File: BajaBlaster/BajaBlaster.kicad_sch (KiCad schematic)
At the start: 0 parts

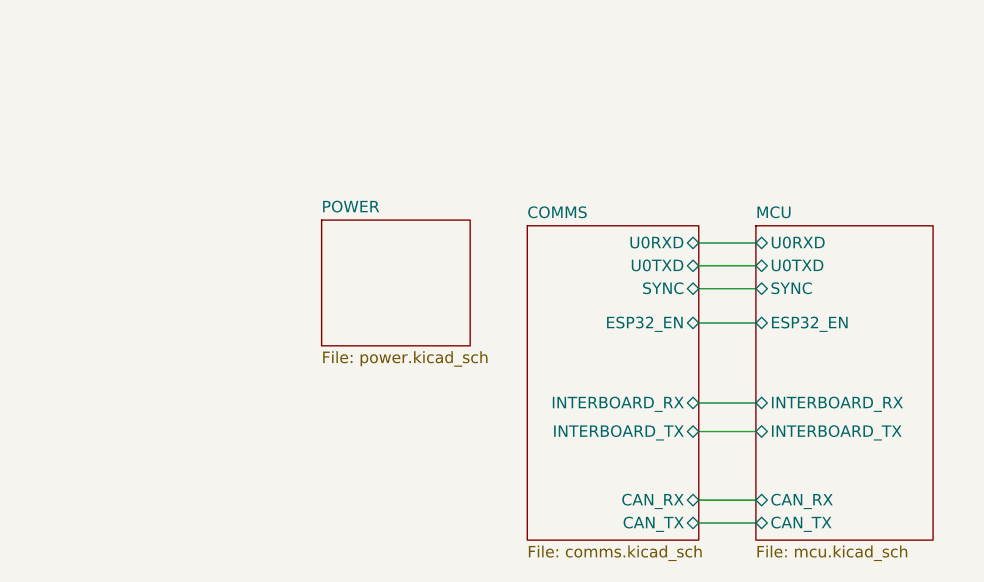
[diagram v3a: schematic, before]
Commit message: added better formatting across schematic
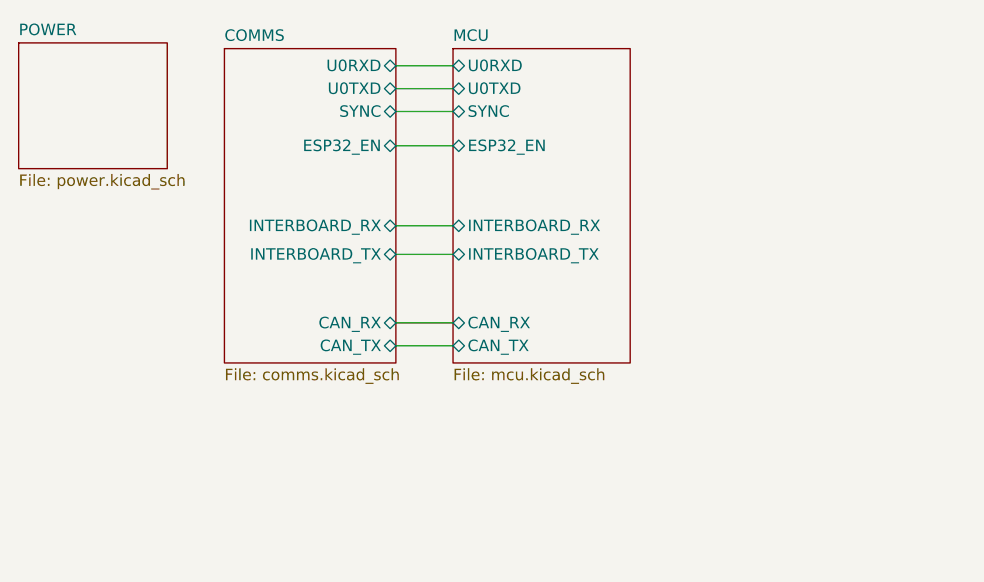
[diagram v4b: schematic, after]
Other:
- company: (none) -> Olin Baja SAE
- title: BAJA_BLASTER_REV_A -> BAJA_BLASTER
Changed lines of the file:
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@@
 	(paper "A5")
 	(title_block
-		(title "BAJA_BLASTER_REV_A")
-	)
-	(wire
-		(pts
-			(xy 99.06 60.96) (xy 105.41 60.96)
-		)
-		(stroke
-			(width 0)
-			(type default)
-		)
-	)
-	(wire
-		(pts
-			(xy 99.06 71.755) (xy 105.41 71.755)
-		)
-		(stroke
-			(width 0)
-			(type default)
-		)
-	)
-	(wire
-		(pts
-			(xy 99.06 48.26) (xy 105.41 48.26)
-		)
-		(stroke
-			(width 0)
-			(type default)
-		)
-	)
-	(wire
-		(pts
-			(xy 99.06 64.135) (xy 105.41 64.135)
-		)
-		(stroke
-			(width 0)
-			(type default)
-		)
-	)
-	(wire
-		(pts
-			(xy 99.06 74.295) (xy 105.41 74.295)
-		)
-		(stroke
-			(width 0)
-			(type default)
-		)
-	)
-	(wire
-		(pts
-			(xy 99.06 52.07) (xy 105.41 52.07)
-		)
-		(stroke
-			(width 0)
-			(type default)
-		)
-	)
-	(wire
-		(pts
-			(xy 99.06 43.18) (xy 105.41 43.18)
-		)
-		(stroke
-			(width 0)
-			(type default)
-		)
-	)
-	(wire
-		(pts
-			(xy 99.06 45.72) (xy 105.41 45.72)
+		(title "BAJA_BLASTER")
+		(date "2026-09-24")
+		(rev "A")
+		(company "Olin Baja SAE")
+	)
+	(wire
+		(pts
+			(xy 65.405 41.275) (xy 71.755 41.275)
+		)
+		(stroke
+			(width 0)
+			(type default)
+		)
+	)
+	(wire
+		(pts
+			(xy 65.405 52.07) (xy 71.755 52.07)
+		)
+		(stroke
+			(width 0)
+			(type default)
+		)
+	)
+	(wire
+		(pts
+			(xy 65.405 28.575) (xy 71.755 28.575)
+		)
+		(stroke
+			(width 0)
+			(type default)
+		)
+	)
+	(wire
+		(pts
+			(xy 65.405 44.45) (xy 71.755 44.45)
+		)
+		(stroke
+			(width 0)
+			(type default)
+		)
+	)
+	(wire
+		(pts
+			(xy 65.405 54.61) (xy 71.755 54.61)
+		)
+		(stroke
+			(width 0)
+			(type default)
+		)
+	)
+	(wire
+		(pts
+			(xy 65.405 32.385) (xy 71.755 32.385)
+		)
+		(stroke
+			(width 0)
+			(type default)
+		)
+	)
+	(wire
+		(pts
+			(xy 65.405 23.495) (xy 71.755 23.495)
+		)
+		(stroke
+			(width 0)
+			(type default)
+		)
+	)
+	(wire
+		(pts
+			(xy 65.405 26.035) (xy 71.755 26.035)
 		)
 		(stroke
@@
 	)
 	(sheet
-		(at 80.01 41.275)
+		(at 46.355 21.59)
 		(size 19.05 34.925)
 		(exclude_from_sim no)
@@
 		)
 		(property "Sheetname" "COMMS"
-			(at 80.01 40.5634 0)
+			(at 46.355 20.8784 0)
 			(show_name no)
 			(do_not_autoplace no)
@@
 		)
 		(property "Sheetfile" "comms.kicad_sch"
-			(at 80.01 76.7846 0)
+			(at 46.355 57.0996 0)
 			(show_name no)
 			(do_not_autoplace no)
@@
 		)
 		(pin "ESP32_EN" bidirectional
-			(at 99.06 52.07 0)
+			(at 65.405 32.385 0)
 			(effects
 				(font
@@
 		)
 		(pin "CAN_TX" bidirectional
-			(at 99.06 74.295 0)
+			(at 65.405 54.61 0)
 			(effects
 				(font
@@
 		)
 		(pin "CAN_RX" bidirectional
-			(at 99.06 71.755 0)
+			(at 65.405 52.07 0)
 			(effects
 				(font
@@
 		)
 		(pin "U0RXD" bidirectional
-			(at 99.06 43.18 0)
+			(at 65.405 23.495 0)
 			(effects
 				(font
@@
 		)
 		(pin "INTERBOARD_RX" bidirectional
-			(at 99.06 60.96 0)
+			(at 65.405 41.275 0)
 			(effects
 				(font
@@
 		)
 		(pin "INTERBOARD_TX" bidirectional
-			(at 99.06 64.135 0)
+			(at 65.405 44.45 0)
 			(effects
 				(font
@@
 		)
 		(pin "U0TXD" bidirectional
-			(at 99.06 45.72 0)
+			(at 65.405 26.035 0)
 			(effects
 				(font
@@
 		)
 		(pin "SYNC" bidirectional
-			(at 99.06 48.26 0)
+			(at 65.405 28.575 0)
 			(effects
 				(font
@@
 	)
 	(sheet
-		(at 57.15 40.64)
+		(at 23.495 20.955)
 		(size 16.51 13.97)
 		(exclude_from_sim no)
@@
 		)
 		(property "Sheetname" "POWER"
-			(at 57.15 39.9284 0)
+			(at 23.495 20.2434 0)
 			(show_name no)
 			(do_not_autoplace no)
@@
 		)
 		(property "Sheetfile" "power.kicad_sch"
-			(at 57.15 55.1946 0)
+			(at 23.495 35.5096 0)
 			(show_name no)
 			(do_not_autoplace no)
@@
 	)
 	(sheet
-		(at 105.41 41.275)
+		(at 71.755 21.59)
 		(size 19.685 34.925)
 		(exclude_from_sim no)
@@
 		)
 		(property "Sheetname" "MCU"
-			(at 105.41 40.5634 0)
+			(at 71.755 20.8784 0)
 			(show_name no)
 			(do_not_autoplace no)
@@
 		)
 		(property "Sheetfile" "mcu.kicad_sch"
-			(at 105.41 76.7846 0)
+			(at 71.755 57.0996 0)
 			(show_name no)
 			(do_not_autoplace no)
@@
 		)
 		(pin "ESP32_EN" bidirectional
-			(at 105.41 52.07 180)
+			(at 71.755 32.385 180)
 			(effects
 				(font
@@
 		)
 		(pin "U0TXD" bidirectional
-			(at 105.41 45.72 180)
+			(at 71.755 26.035 180)
 			(effects
 				(font
@@
 		)
 		(pin "U0RXD" bidirectional
-			(at 105.41 43.18 180)
+			(at 71.755 23.495 180)
 			(effects
 				(font
@@
 		)
 		(pin "INTERBOARD_RX" bidirectional
-			(at 105.41 60.96 180)
+			(at 71.755 41.275 180)
 			(effects
 				(font
@@
 		)
 		(pin "INTERBOARD_TX" bidirectional
-			(at 105.41 64.135 180)
+			(at 71.755 44.45 180)
 			(effects
 				(font
@@
 		)
 		(pin "CAN_RX" bidirectional
-			(at 105.41 71.755 180)
+			(at 71.755 52.07 180)
 			(effects
 				(font
@@
 		)
 		(pin "CAN_TX" bidirectional
-			(at 105.41 74.295 180)
+			(at 71.755 54.61 180)
 			(effects
 				(font
@@
 		)
 		(pin "SYNC" bidirectional
-			(at 105.41 48.26 180)
-			(effects
-				(font
+			(at 71.755 28.575 180)
+			(effects
+				(font

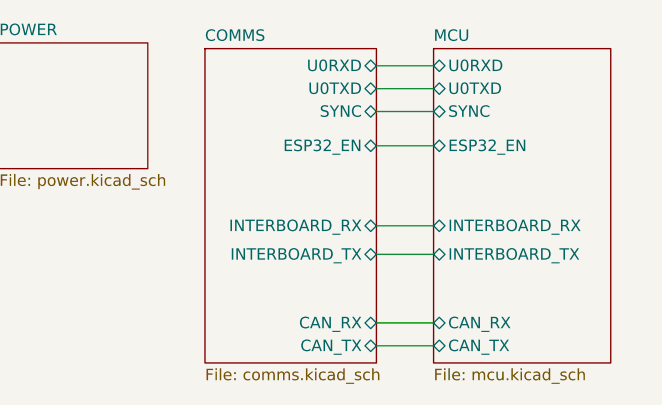
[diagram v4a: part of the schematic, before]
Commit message: passed erc with no errors just hella warnings
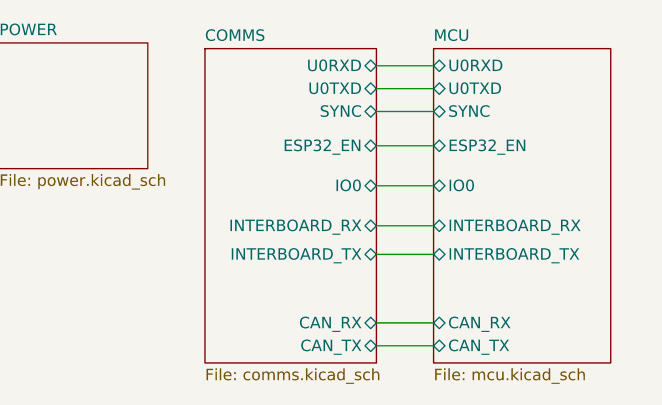
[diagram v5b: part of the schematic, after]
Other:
- sheet COMMS ports: added IO0; removed none
- sheet MCU ports: added IO0; removed none
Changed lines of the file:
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@@
+		)
+	)
+	(wire
+		(pts
+			(xy 65.405 36.83) (xy 71.755 36.83)
+		)
+		(stroke
+			(width 0)
+			(type default)
 		)
 	)
@@
 			)
 		)
+		(pin "IO0" bidirectional
+			(at 65.405 36.83 0)
+			(effects
+				(font
+					(size 1.27 1.27)
+				)
+				(justify right)
+			)
+		)
 		(instances
 			(project "BajaBlaster"
@@
 			(effects
 				(font
+					(size 1.27 1.27)
+				)
+				(justify left)
+			)
+		)
+		(pin "IO0" bidirectional
+			(at 71.755 36.83 180)
+			(effects
+				(font

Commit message: sendoff
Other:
- sheet COMMS ports: added EXT_CAN_RX, EXT_CAN_TX, INTER_CAN_RX, INTER_CAN_TX, NRST, SWCLK, SWDIO, SWO; removed CAN_RX, CAN_TX, ESP32_EN, INTERBOARD_RX, INTERBOARD_TX, IO0, SYNC, U0RXD, U0TXD
- sheet MCU ports: added EXT_CAN_RX, EXT_CAN_TX, INTER_CAN_RX, INTER_CAN_TX, NRST, SWCLK, SWDIO, SWO; removed CAN_RX, CAN_TX, ESP32_EN, INTERBOARD_RX, INTERBOARD_TX, IO0, SYNC, U0RXD, U0TXD
